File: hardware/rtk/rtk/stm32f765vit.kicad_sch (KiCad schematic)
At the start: 30 parts, among them J10 Conn_01x02_Pin, J6 MEM2052-00-195-00-A_REVA, J7 Conn_01x04_Pin, J8 Conn_01x01_Pin, J9 Conn_01x08_Pin, U3 STM32F765VITx, U5 ESP32-S3-ZERO, U6 CORE1262-868M, U7 LSM6DSOX, Y1 ASTX-H11-16.000MHZ-T

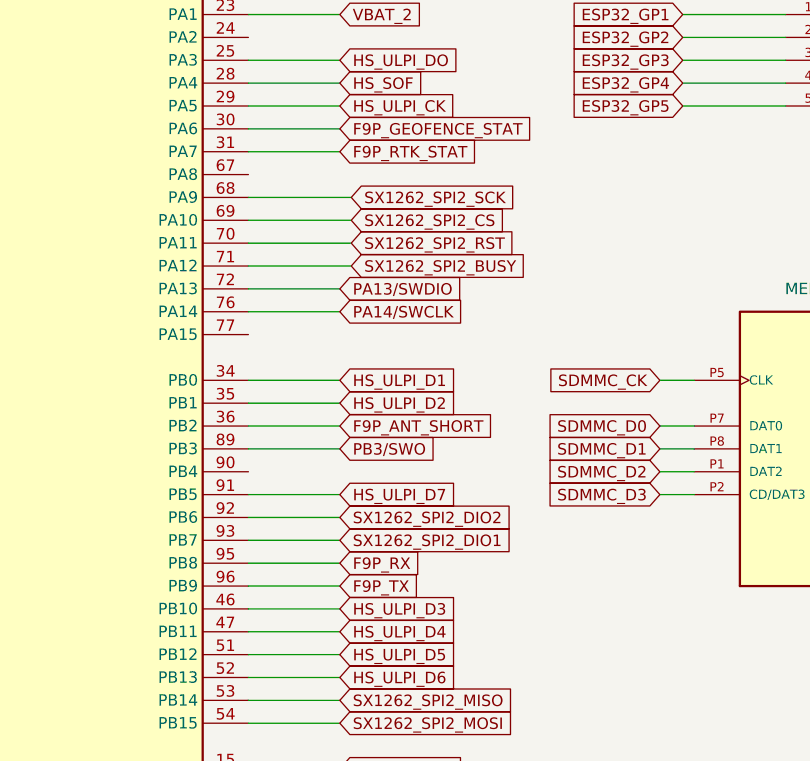
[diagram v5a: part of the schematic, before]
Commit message: Connect F9P UART2 (corrections port) to STM32 UART7
PA8 (UART7_RX) → F9P TXD2, PA15 (UART7_TX) → F9P RXD2.
Dedicated channel for RTCM correction data, keeping UART1 free
for navigation output and UBX configuration.

Co-Authored-By: Claude Sonnet 4.6 <noreply@anthropic.com>
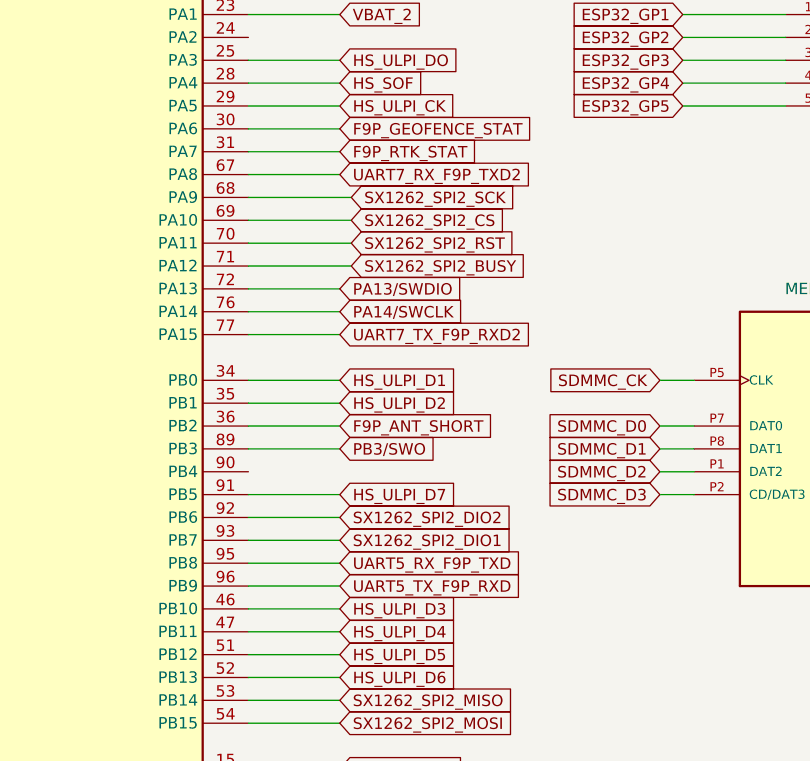
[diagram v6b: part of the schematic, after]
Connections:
- net UART7_RX_F9P_TXD2: now reaches U3.67 (PA8)
- net UART7_TX_F9P_RXD2: now reaches U3.77 (PA15)
- net F9P_RX renamed UART5_RX_F9P_TXD
- net F9P_TX renamed UART5_TX_F9P_RXD
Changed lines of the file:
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@@
 	(wire
 		(pts
+			(xy 153.67 78.74) (xy 163.83 78.74)
+		)
+		(stroke
+			(width 0)
+			(type default)
+		)
+	)
+	(wire
+		(pts
 			(xy 96.52 50.8) (xy 96.52 45.72)
 		)
@@
 	(wire
 		(pts
+			(xy 153.67 60.96) (xy 163.83 60.96)
+		)
+		(stroke
+			(width 0)
+			(type default)
+		)
+	)
+	(wire
+		(pts
 			(xy 27.94 157.48) (xy 39.37 157.48)
 		)
@@
 		)
 	)
+	(global_label "UART7_TX_F9P_RXD2"
+		(shape input)
+		(at 163.83 78.74 0)
+		(fields_autoplaced yes)
+		(effects
+			(font
+				(size 1.27 1.27)
+			)
+			(justify left)
+		)
+		(property "Intersheetrefs" "${INTERSHEET_REFS}"
+			(at 186.2884 78.74 0)
+			(hide yes)
+			(show_name no)
+			(do_not_autoplace no)
+			(effects
+				(font
+					(size 1.27 1.27)
+				)
+				(justify left)
+			)
+		)
+	)
 	(global_label "SX1262_SPI2_CS"
 		(shape input)
@@
 		)
 	)
-	(global_label "F9P_TX"
+	(global_label "UART5_TX_F9P_RXD"
 		(shape input)
 		(at 163.83 106.68 0)
@@
 		)
 		(property "Intersheetrefs" "${INTERSHEET_REFS}"
-			(at 173.528 106.68 0)
+			(at 185.0789 106.68 0)
 			(hide yes)
 			(show_name no)
@@
 		)
 	)
-	(global_label "F9P_RX"
+	(global_label "UART5_RX_F9P_TXD"
 		(shape input)
 		(at 163.83 104.14 0)
@@
 		)
 		(property "Intersheetrefs" "${INTERSHEET_REFS}"
-			(at 173.8304 104.14 0)
+			(at 185.0789 104.14 0)
 			(hide yes)
 			(show_name no)
@@
 			(hide yes)
 			(show_name no)
+			(do_not_autoplace no)
+			(effects
+				(font
+					(size 1.27 1.27)
+				)
+				(justify left)
+			)
+		)
+	)
+	(global_label "UART7_RX_F9P_TXD2"
+		(shape input)
+		(at 163.83 60.96 0)
+		(fields_autoplaced yes)
+		(effects
+			(font
+				(size 1.27 1.27)
+			)
+			(justify left)
+		)
+		(property "Intersheetrefs" "${INTERSHEET_REFS}"
+			(at 186.2884 60.96 0)
+			(hide yes)
+			(show_name no)

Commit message: Schematic/PCB/ioc: mode-select jumper, ESD swap, routing updates
PA0 (BASE_ROVER_MODE_SELECT) added to ioc with pull-up, FB1 removed
from schematic, USBLC6-4SC6 replaces out-of-stock USBLC6-2SC6,
PCB routing updates from design review session.

Co-Authored-By: Claude Sonnet 4.6 <noreply@anthropic.com>
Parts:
- added J12: Conn_01x02_Pin, Connector_PinHeader_2.54mm:PinHeader_1x02_P2.54mm_Vertical, symbol Connector:Conn_01x02_Pin
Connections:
- net GND: now also J12.1 (Pin_1)
- net at U3.22 (PA0): now also J12.2 (Pin_2)
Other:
- note added: "Base/Rover Mode Select Open is Base"
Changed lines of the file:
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@@
 	(generator_version "10.0")
 	(paper "A4")
+	(text "Base/Rover\nMode Select\nOpen is Base"
+		(exclude_from_sim no)
+		(at 185.928 28.194 0)
+		(effects
+			(font
+				(size 1.27 1.27)
+			)
+		)
+	)
 	(text "STM32 Decouploing capacitors"
 		(exclude_from_sim no)
@@
 	(wire
 		(pts
+			(xy 165.1 29.21) (xy 168.91 29.21)
+		)
+		(stroke
+			(width 0)
+			(type default)
+		)
+	)
+	(wire
+		(pts
 			(xy 57.15 96.52) (xy 63.5 96.52)
 		)
@@
 	(wire
 		(pts
+			(xy 165.1 29.21) (xy 165.1 31.75)
+		)
+		(stroke
+			(width 0)
+			(type default)
+		)
+	)
+	(wire
+		(pts
 			(xy 27.94 157.48) (xy 39.37 157.48)
 		)
@@
 	(wire
 		(pts
+			(xy 153.67 40.64) (xy 158.75 40.64)
+		)
+		(stroke
+			(width 0)
+			(type default)
+		)
+	)
+	(wire
+		(pts
 			(xy 16.51 81.28) (xy 21.59 81.28)
 		)
@@
 	(wire
 		(pts
+			(xy 158.75 26.67) (xy 168.91 26.67)
+		)
+		(stroke
+			(width 0)
+			(type default)
+		)
+	)
+	(wire
+		(pts
 			(xy 257.81 125.73) (xy 257.81 130.81)
 		)
@@
 	(wire
 		(pts
+			(xy 158.75 26.67) (xy 158.75 40.64)
+		)
+		(stroke
+			(width 0)
+			(type default)
+		)
+	)
+	(wire
+		(pts
 			(xy 99.06 101.6) (xy 107.95 101.6)
 		)
@@
 	)
 	(symbol
+		(lib_id "Connector:Conn_01x02_Pin")
+		(at 173.99 29.21 180)
+		(unit 1)
+		(body_style 1)
+		(exclude_from_sim no)
+		(in_bom yes)
+		(on_board yes)
+		(in_pos_files yes)
+		(dnp no)
+		(property "Reference" "J12"
+			(at 175.514 27.94 0)
+			(show_name no)
+			(do_not_autoplace no)
+			(effects
+				(font
+					(size 1.27 1.27)
+				)
+				(justify right)
+			)
+		)
+		(property "Value" "Conn_01x02_Pin"
+			(at 175.26 29.2099 0)
+			(hide yes)
+			(show_name no)
+			(do_not_autoplace no)
+			(effects
+				(font
+					(size 1.27 1.27)
+				)
+				(justify right)
+			)
+		)
+		(property "Footprint" "Connector_PinHeader_2.54mm:PinHeader_1x02_P2.54mm_Vertical"
+			(at 173.99 29.21 0)
+			(hide yes)
+			(show_name no)
+			(do_not_autoplace no)
+			(effects
+				(font
+					(size 1.27 1.27)
+				)
+			)
+		)
+		(property "Datasheet" ""
+			(at 173.99 29.21 0)
+			(hide yes)
+			(show_name no)
+			(do_not_autoplace no)
+			(effects
+				(font
+					(size 1.27 1.27)
+				)
+			)
+		)
+		(property "Description" "Generic connector, single row, 01x02, script generated"
+			(at 173.99 29.21 0)
+			(hide yes)
+			(show_name no)
+			(do_not_autoplace no)
+			(effects
+				(font
+					(size 1.27 1.27)
+				)
+			)
+		)
+		(pin "1"
+		)
+		(pin "2"
+		)
+		(instances
+			(project "rtk"
+				(path "/608e0f5f-bf55-4b10-9802-aab1430116aa/f27ee638-88fe-42f5-8480-7c3da399fb44"
+					(reference "J12")
+					(unit 1)
+				)
+			)
+		)
+	)
+	(symbol
 		(lib_id "Device:C_Small")
 		(at 21.59 182.88 0)
@@
 					(unit 1)
 				)
+			)
+		)
+	)
+	(symbol
+		(lib_id "power:GND")
+		(at 165.1 31.75 0)
+		(unit 1)
+		(body_style 1)
+		(exclude_from_sim no)
+		(in_bom yes)
+		(on_board yes)
+		(in_pos_files yes)
+		(dnp no)
+		(property "Reference" "#PWR043"
+			(at 165.1 38.1 0)
+			(hide yes)
+			(show_name no)
+			(do_not_autoplace no)
+			(effects
+				(font
+					(size 1.27 1.27)
+				)
+			)
+		)
+		(property "Value" "GND"
+			(at 168.402 33.782 0)
+			(show_name no)
+			(do_not_autoplace no)
+			(effects
+				(font
+					(size 1.27 1.27)
+				)
+			)
+		)
+		(property "Footprint" ""
+			(at 165.1 31.75 0)
+			(hide yes)
+			(show_name no)
+			(do_not_autoplace no)
+			(effects
+				(font
+					(size 1.27 1.27)
+				)
+			)
+		)
+		(property "Datasheet" ""
+			(at 165.1 31.75 0)
+			(hide yes)
+			(show_name no)
+			(do_not_autoplace no)
+			(effects
+				(font
+					(size 1.27 1.27)
+				)
+			)
+		)
+		(property "Description" "Power symbol creates a global label with name \"GND\" , ground"
+			(at 165.1 31.75 0)
+			(hide yes)
+			(show_name no)
+			(do_not_autoplace no)
+			(effects
+				(font
+					(size 1.27 1.27)
+				)
+			)
+		)
+		(pin "1"
+		)
+		(instances
+			(project "rtk"
+				(path "/608e0f5f-bf55-4b10-9802-aab1430116aa/f27ee638-88fe-42f5-8480-7c3da399fb44"
+					(reference "#PWR043")
+					(unit 1)
+				)
